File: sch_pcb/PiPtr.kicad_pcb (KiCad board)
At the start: 4 copper layers, 101.6 x 141.7 mm, 383 parts, among them J101 GLOBAL_LINK_LEFT, J102 GLOBAL_LINK_RIGHT, J107 RASPBERRY_PI, J111 FP_PIXEL, J112 AM2302, J204 DE9F, J305 AUX_IO_1, J307 SPARE, J308 AUX_IO_2, J311 I2C1_5V, J312 RTC, J315 OLED_SSD1306, J404 DE9F, J501 MicroUSB, P301 Chassis, Q101 BSS138, Q102 BSS138, Q103 BSS138, Q104 BSS138, Q105 BSS138, Q201 BSS138, Q202 BSS138, Q203 BSS138, Q401 BSS138, Q402 BSS138, Q403 BSS138, Q501 BSR315PH6327XTSA1, U101 MCP23008, U102 IP4234CZ6, U103 MCP4351, U104 74HCT138, U105 74LV1T125, U106 MCP6004T, U107 MCP4351, U108 74LVC4066, U109 74LVC1G3157, U110 74LV1T125, U111 74LV1T125, U112 74LV1T125, U113 74LV1T125, U201 MCP6004T, U202 74LVC1G3157, U203 74LVC1G3157, U204 74LVC4066, U205 MCP6004T, U206 74LVC1G3157, U207 MCP6S26, U208 MCP23008, U301 MCP23017, U304 MCP3008, U305 MCP1703A-2502/MB, U306 TPS54302, U307 IP4234CZ6, U308 IP4234CZ6, U401 MCP6004T, U402 74LVC1G3157, U403 74LVC1G3157, U404 74LVC4066, U405 MCP6004T, U406 74LVC1G3157, U407 MCP6S26, U408 MCP23008, U501 CM108B, U502 CM108B, U503 TUSB2036, U504 MCP1703A-3302/MB, U505 CM108B, Y501 6MHz

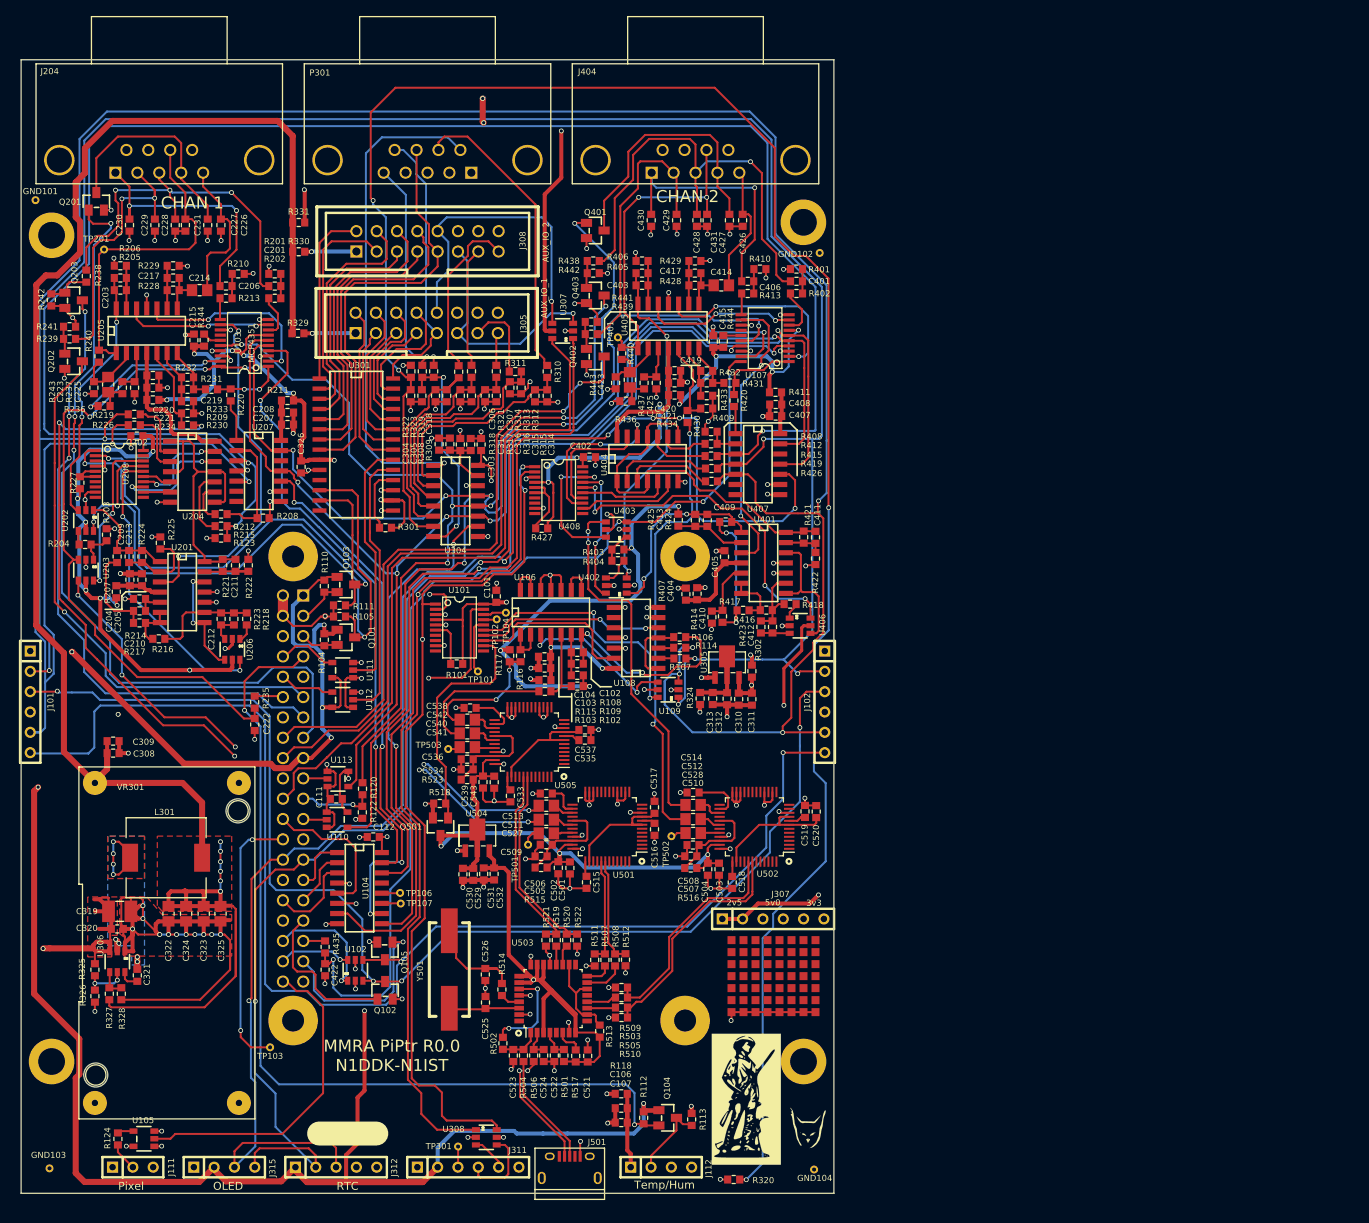
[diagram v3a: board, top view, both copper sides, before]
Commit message: Add files via upload
Fix i2c addressing
Change footprint for LDR
Move connectors for temp/hum sensor and rtc so they won't hit the Pi
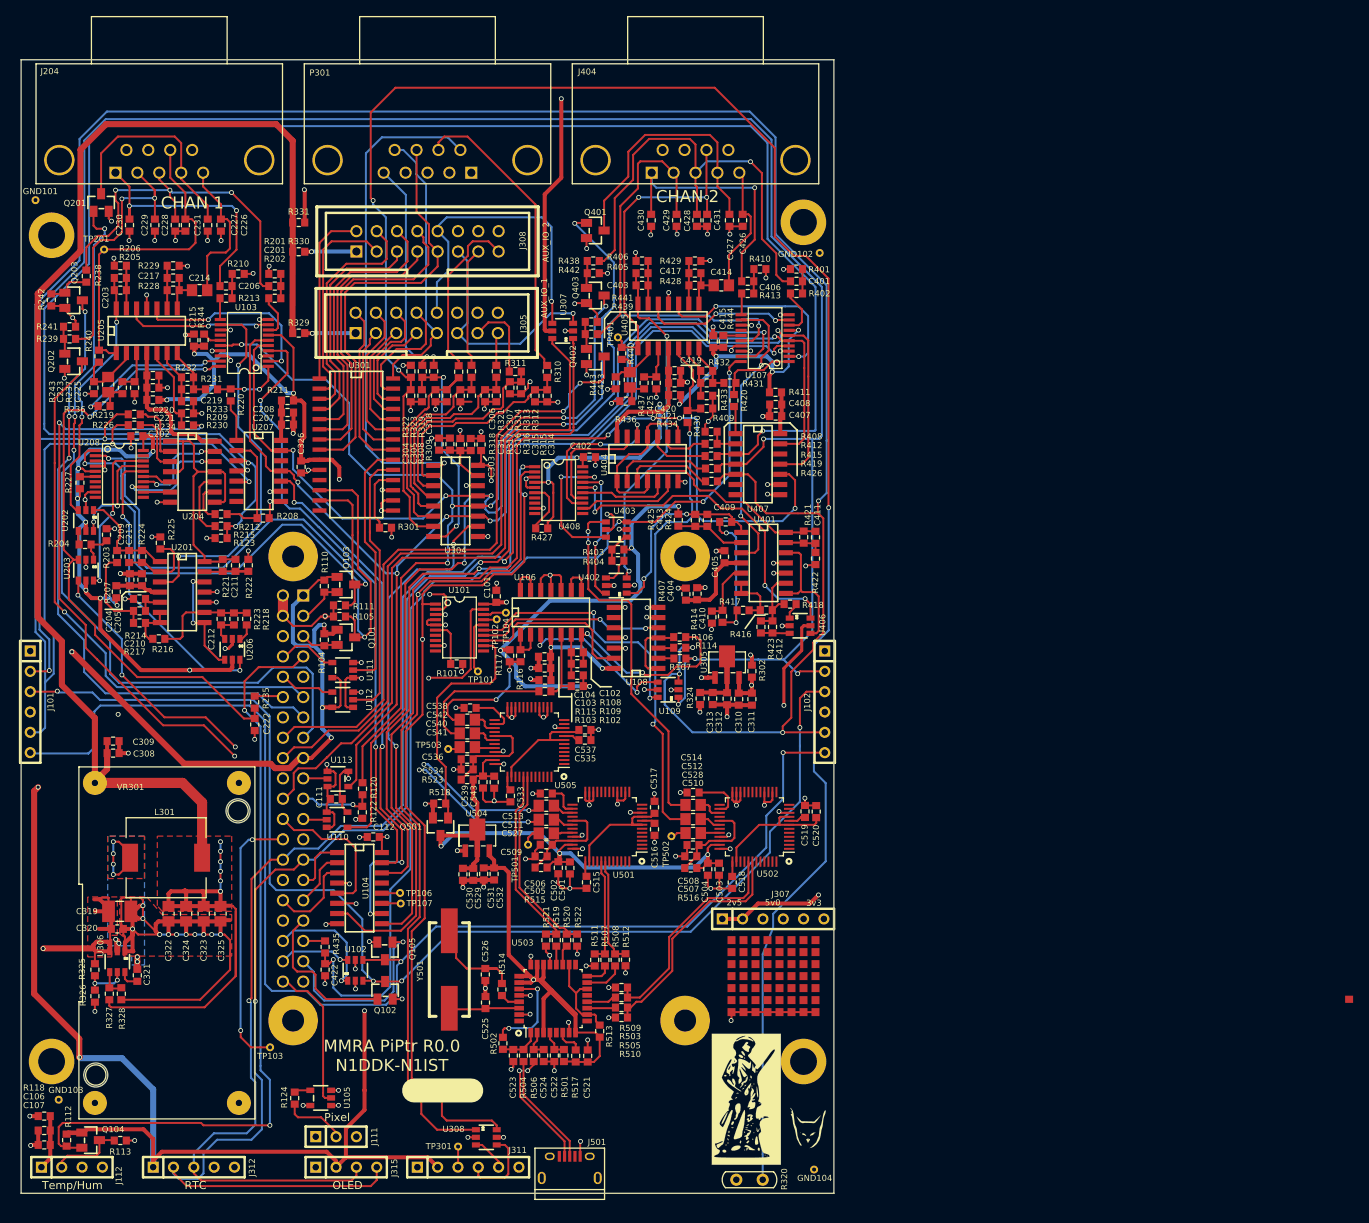
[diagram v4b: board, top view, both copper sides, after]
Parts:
- R216, R218, R416, R418: value 50k -> 51k
- R310, R311, R312, R313, R314, R321: value 90k -> 88k7
- R320: footprint lib:smd0603 -> lib:LDR
- moved J112 73.7 mm to (63.5, 166.4)
- moved C106 72.2 mm to (60.0, 161.8)
- moved C107 72.2 mm to (60.0, 163.6)
- moved Q104 72.2 mm to (65.8, 163.0)
- moved R112 72.2 mm to (62.8, 163.0)
- moved R118 72.2 mm to (60.0, 160.0)
- moved R113 71.5 mm to (69.5, 163.0), turned to 0 degrees
- moved J111 25.7 mm to (96.5, 162.6)
- moved R124 22.7 mm to (91.3, 157.7)
- moved U105 22.7 mm to (94.6, 157.7)
- moved J312 17.8 mm to (80.0, 166.4)
- moved J315 15.2 mm to (97.8, 166.4)
- moved GND103 8.65 mm to (61.9, 157.9)
- moved R320 1.98 mm to (148.2, 167.9), turned to 0 degrees
- moved Q201 0.62 mm to (67.2, 45.8)
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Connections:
- U101 pad 5: GND -> +5V
- U208 pad 5: Net-(R227-Pad1) -> +5V
- U301 pad 16: +5V -> GND
- U301 pad 17: GND -> +5V
- U408 pad 5: Net-(R427-Pad1) -> GND
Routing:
- net /SDA0_33: track 148.0 -> 173.9 mm
- net +3V3: track 561.9 -> 537.2 mm, vias 11 -> 9
- net /PIXEL_33: track 40.9 -> 19.3 mm
- net /DHT_33: track 113.4 -> 97.9 mm
- net /SCL0_33: track 154.3 -> 163.8 mm
- net +5V: track 531.0 -> 523.6 mm, vias 46 -> 47
- net Net-(J111-Pad2): track 3.55 -> 7.91 mm
- net /CH1/TONE_FROM_PI: track 83.4 -> 79.2 mm, vias 3 -> 2
- net GND: track 367.9 -> 370.4 mm, vias 155 -> 153
- net Net-(C106-Pad1): track 11.1 -> 8.64 mm
- net Net-(R227-Pad1): track 4.14 -> 1.93 mm
- net /Spares, GPIO, and ADC/ADC_LIGHT: track 251.8 -> 249.7 mm, vias 4 -> 3
- net Net-(R427-Pad1): track 8.46 -> 6.62 mm
- net /PTT1D: track 101.2 -> 99.3 mm
- net Net-(R208-Pad2): track 16.2 -> 14.5 mm
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
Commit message: Add Digikey part # to all parts.  Fix unconnected nets
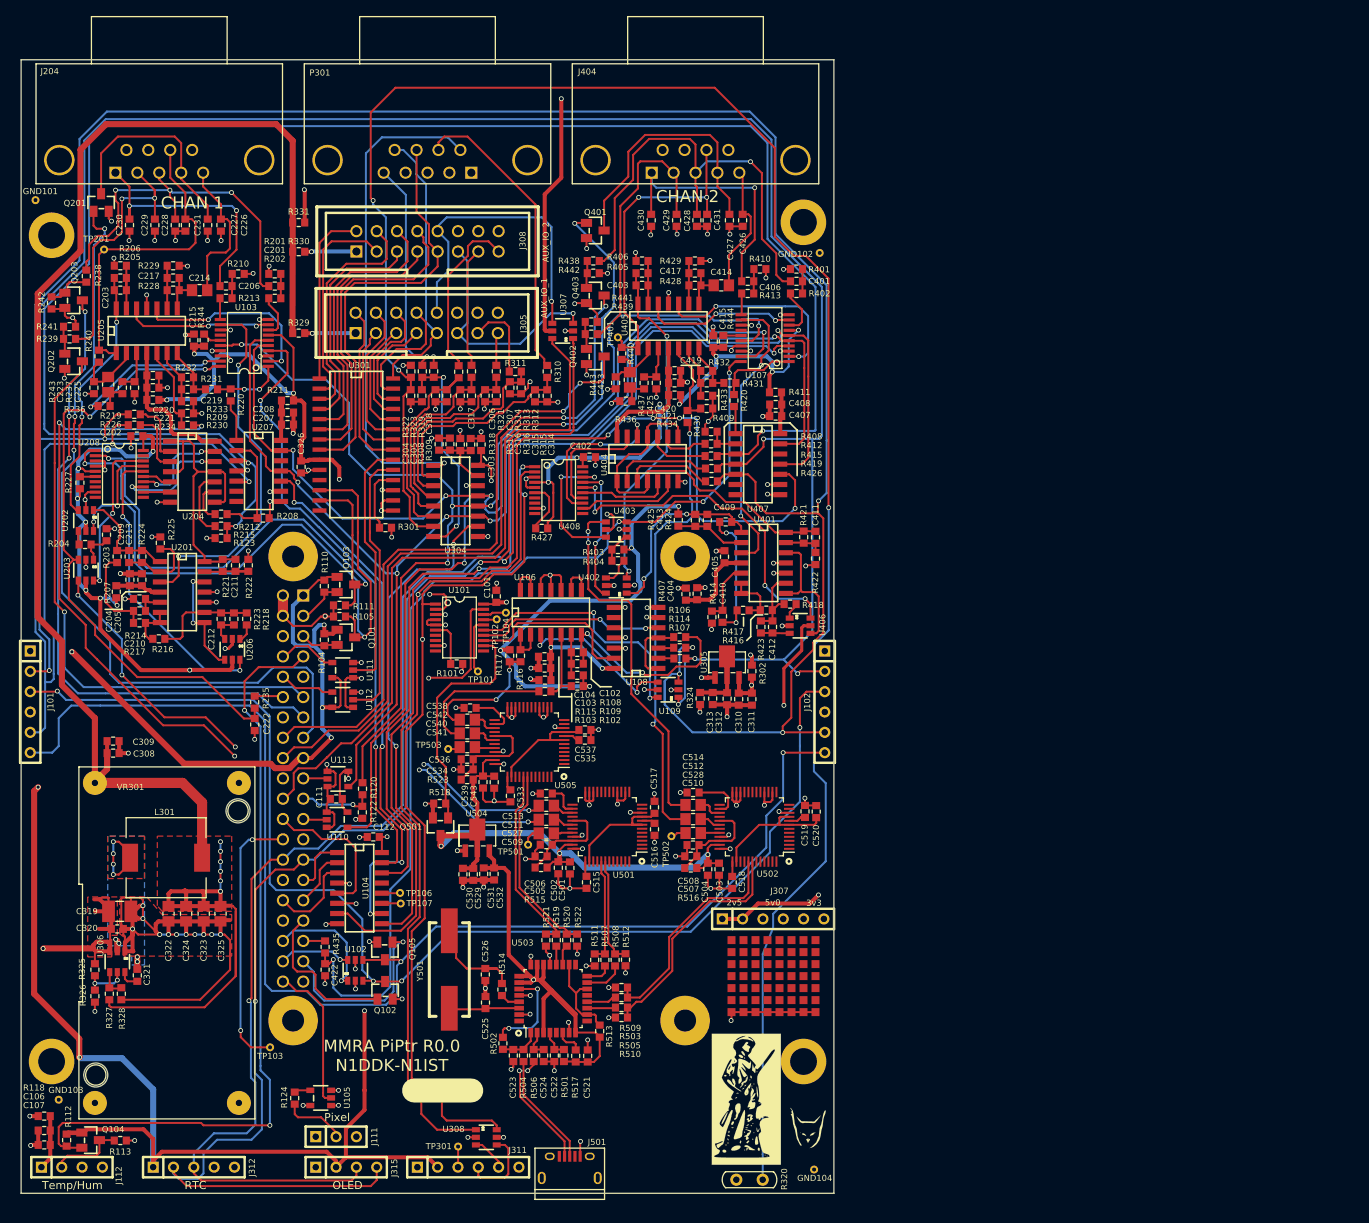
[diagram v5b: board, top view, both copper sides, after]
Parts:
- Q501: value BSR315PH6327XTSA1 -> NX2301P,215
- moved R242 0.38 mm to (61.0, 58.3)
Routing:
- net +2V5: track 152.7 -> 147.0 mm, vias 39 -> 38
- net +5V: track 523.6 -> 526.2 mm
- net /COR1: track 69.2 -> 71.6 mm
- net /~CTCSS1: track 79.1 -> 81.1 mm
- net GND: track 370.4 -> 371.4 mm

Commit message: Switch to 0402 parts and SeeedStudio footprints
Silk screen is still being updated.  BOM needs to be updated as well
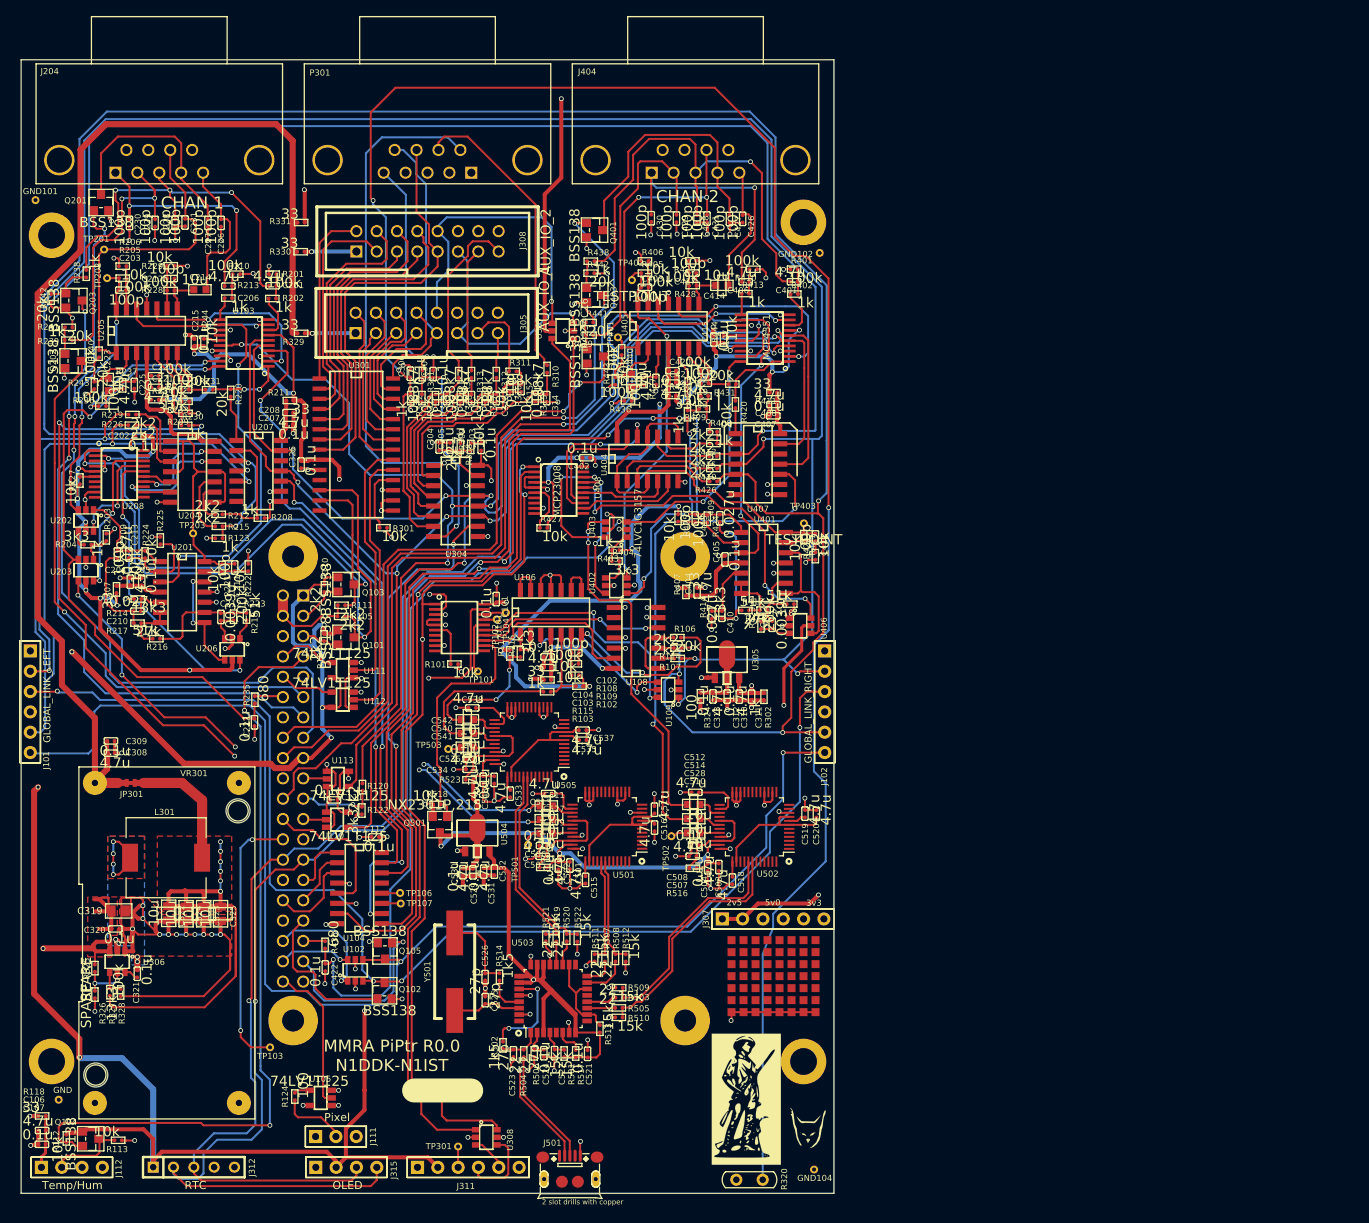
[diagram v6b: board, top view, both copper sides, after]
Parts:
- added JP301: 5V_switcher_connect, lib:JUMPER_2PIN_CUTTABLE, F.Cu at (70.8, 118.3)
- added TP202: TESTPOINT, lib:Wire_28AWG, F.Cu at (67.9, 55.2)
- added TP203: TESTPOINT, lib:Wire_28AWG, F.Cu at (78.7, 87.1)
- added TP402: TESTPOINT, lib:Wire_28AWG, F.Cu at (133.5, 55.5)
- added TP403: TESTPOINT, lib:Wire_28AWG, F.Cu at (155.0, 85.9)
- C101, C102, C103, C104, C106, C107, C111, C112, C201, C202, C203, C204, C205, C206, C207, C208, C209, C210, C211, C212, C213, C215, C217, C219, C220, C221, C222, C225, C226, C227, C228, C229, C230, C231, C303, C304, C305, C306, C307, C308, C309, C310, C311, C312, C313, C314, C315, C316, C317, C318, C320, C321, C326, C401, C402, C403, C404, C405, C406, C407, C408, C409, C410, C411, C412, C413, C415, C417, C419, C420, C421, C422, C425, C426, C427, C428, C429, C430, C431, C501, C502, C503, C504, C505, C506, C507, C508, C513, C514, C515, C516, C517, C518, C519, C520, C521, C522, C523, C524, C525, C526, C529, C530, C531, C532, C533, C534, C535, C536, C537, C538, C539, C543: footprint lib:smd0603 -> lib:OPL_C0402
- C214, C223, C414, C423, C509, C510, C511, C512, C527, C528, C540, C541, C542: footprint lib:smd0805 -> lib:OPL_C0603
- C319: footprint lib:smd1210 -> lib:OPL_C0805
- C322, C323, C324, C325: footprint lib:smd0805 -> lib:OPL_C0805
- J101, J102, J307, J311: footprint lib:SIL-6 -> lib:OPL_H6-2.54
- J111: footprint lib:SIL-3 -> lib:OPL_H3-2.54
- J112, J315: footprint lib:SIL-4 -> lib:OPL_H4-2.54
- J501: footprint lib:USB_Micro-B -> lib:OPL_MICRO-USB5+4P-SMD-0.65-B
- Q101, Q102, Q103, Q104, Q105, Q201, Q202, Q203, Q401, Q402, Q403, Q501: footprint lib:SOT23 -> lib:OPL_SOT-23
- R101, R102, R103, R104, R105, R106, R107, R108, R109, R110, R111, R112, R113, R114, R115, R116, R117, R118, R120, R122, R123, R124, R201, R202, R203, R204, R205, R206, R207, R208, R209, R210, R211, R212, R213, R214, R215, R216, R217, R218, R219, R220, R221, R222, R223, R224, R225, R226, R227, R228, R229, R230, R231, R232, R233, R234, R235, R236, R237, R238, R239, R240, R241, R242, R243, R244, R301, R302, R308, R309, R310, R311, R312, R313, R314, R315, R316, R317, R318, R319, R321, R322, R323, R324, R325, R326, R327, R328, R329, R330, R331, R401, R402, R403, R404, R405, R406, R407, R408, R409, R410, R411, R412, R413, R414, R415, R416, R417, R418, R419, R420, R421, R422, R423, R424, R425, R426, R427, R428, R429, R430, R431, R432, R433, R434, R435, R436, R437, R438, R439, R440, R441, R442, R443, R444, R501, R502, R503, R504, R505, R506, R507, R508, R509, R510, R511, R512, R513, R514, R515, R516, R517, R518, R519, R520, R521, R522, R523: footprint lib:smd0603 -> lib:OPL_R0402
- U101, U103, U107, U208, U408: footprint lib:SSOP-20 -> lib:OPL_TSSOP20-0.65-6.5X4.4MM
- U102, U109, U202, U203, U206, U306, U307, U308, U402, U403, U406: footprint lib:SOT23-6 -> lib:OPL_SOT-23-6
- U105, U110, U111, U112, U113: footprint lib:SOT23-5 -> lib:OPL_SOT-23-5
- U305, U504: footprint lib:sot89 -> lib:OPL_SOT-89
- moved R302 3.54 mm to (150.0, 107.6), turned to 0 degrees
- moved J501 1.68 mm to (125.8, 164.7)
- moved R514 1.61 mm to (117.0, 142.6), turned to 180 degrees
- moved C409 0.87 mm to (144.5, 85.3)
- moved R410 0.83 mm to (148.7, 54.1), turned to 270 degrees
- moved Y501 0.73 mm to (111.3, 141.9)
- moved R242 0.65 mm to (60.9, 57.7), turned to 0 degrees
- moved R420 0.53 mm to (146.4, 71.0), turned to 0 degrees
- moved R224 0.47 mm to (72.7, 89.8), turned to 0 degrees
- moved R409 0.47 mm to (142.4, 71.6), turned to 270 degrees
- moved C403 0.44 mm to (135.1, 56.4), turned to 90 degrees
- moved C506 0.42 mm to (122.4, 126.2), turned to 270 degrees
- moved C402 0.41 mm to (127.8, 77.7), turned to 270 degrees
- moved R518 0.39 mm to (109.1, 121.0), turned to 270 degrees
- moved C104 0.39 mm to (123.0, 102.6), turned to 270 degrees
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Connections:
- C322 pad 1: +5V -> Net-(C322-Pad1)
- C323 pad 1: +5V -> Net-(C322-Pad1)
- C324 pad 1: +5V -> Net-(C322-Pad1)
- C325 pad 1: +5V -> Net-(C322-Pad1)
- J305 pad 16: Net-(J305-Pad16) -> (no net)
- J308 pad 16: Net-(J308-Pad16) -> (no net)
- J312 pad 4: (no net) -> Net-(J312-Pad4)
- L301 pad 1: +5V -> Net-(C322-Pad1)
- MTG301 pad 1: Net-(MTG301-Pad1) -> (no net)
- MTG302 pad 1: Net-(MTG302-Pad1) -> (no net)
- MTG303 pad 1: Net-(MTG303-Pad1) -> (no net)
- MTG304 pad 1: Net-(MTG304-Pad1) -> (no net)
- R327 pad 1: +5V -> Net-(C322-Pad1)
- U101 pad 10: (no net) -> Net-(U101-Pad10)
- U101 pad 11: (no net) -> Net-(U101-Pad11)
- U101 pad 7: (no net) -> Net-(U101-Pad7)
- U101 pad 8: (no net) -> Net-(U101-Pad8)
- U104 pad 13: Net-(U104-Pad13) -> (no net)
- U108 pad 10: (no net) -> Net-(U108-Pad10)
- U108 pad 9: (no net) -> Net-(U108-Pad9)
- U207 pad 12: Net-(U207-Pad12) -> (no net)
- U207 pad 6: Net-(U207-Pad6) -> (no net)
- U207 pad 7: Net-(U207-Pad7) -> (no net)
- U208 pad 10: (no net) -> Net-(U208-Pad10)
- U208 pad 11: (no net) -> Net-(U208-Pad11)
- U208 pad 19: (no net) -> Net-(U208-Pad19)
- U208 pad 7: (no net) -> Net-(U208-Pad7)
- U208 pad 8: (no net) -> Net-(U208-Pad8)
- U407 pad 12: Net-(U407-Pad12) -> (no net)
- U407 pad 6: Net-(U407-Pad6) -> (no net)
- U407 pad 7: Net-(U407-Pad7) -> (no net)
- U501 pad 1: Net-(U501-Pad1) -> (no net)
- U501 pad 11: Net-(U501-Pad11) -> (no net)
- U501 pad 12: Net-(U501-Pad12) -> (no net)
- U501 pad 13: Net-(U501-Pad13) -> (no net)
- U501 pad 15: Net-(U501-Pad15) -> (no net)
- U501 pad 17: Net-(U501-Pad17) -> (no net)
- U501 pad 18: Net-(U501-Pad18) -> (no net)
- U501 pad 19: Net-(U501-Pad19) -> (no net)
- U501 pad 2: Net-(U501-Pad2) -> (no net)
- U501 pad 20: Net-(U501-Pad20) -> (no net)
- U501 pad 21: Net-(U501-Pad21) -> (no net)
- U501 pad 25: Net-(U501-Pad25) -> (no net)
- U501 pad 28: Net-(U501-Pad28) -> (no net)
- U501 pad 3: Net-(U501-Pad3) -> (no net)
- U501 pad 31: Net-(U501-Pad31) -> (no net)
- U501 pad 39: Net-(U501-Pad39) -> (no net)
- U501 pad 4: Net-(U501-Pad4) -> (no net)
- U501 pad 40: Net-(U501-Pad40) -> (no net)
- U501 pad 43: Net-(U501-Pad43) -> (no net)
- U501 pad 44: Net-(U501-Pad44) -> (no net)
- U501 pad 45: Net-(U501-Pad45) -> (no net)
- U501 pad 46: Net-(U501-Pad46) -> (no net)
- U501 pad 47: Net-(U501-Pad47) -> (no net)
- U501 pad 48: Net-(U501-Pad48) -> (no net)
- U501 pad 5: Net-(U501-Pad5) -> (no net)
- U501 pad 6: Net-(U501-Pad6) -> (no net)
- U502 pad 1: Net-(U502-Pad1) -> (no net)
- U502 pad 11: Net-(U502-Pad11) -> (no net)
- U502 pad 12: Net-(U502-Pad12) -> (no net)
- U502 pad 13: Net-(U502-Pad13) -> (no net)
- U502 pad 15: Net-(U502-Pad15) -> (no net)
- U502 pad 17: Net-(U502-Pad17) -> (no net)
- U502 pad 18: Net-(U502-Pad18) -> (no net)
- U502 pad 19: Net-(U502-Pad19) -> (no net)
- U502 pad 2: Net-(U502-Pad2) -> (no net)
- U502 pad 20: Net-(U502-Pad20) -> (no net)
- U502 pad 21: Net-(U502-Pad21) -> (no net)
- U502 pad 25: Net-(U502-Pad25) -> (no net)
- U502 pad 28: Net-(U502-Pad28) -> (no net)
- U502 pad 3: Net-(U502-Pad3) -> (no net)
- U502 pad 31: Net-(U502-Pad31) -> (no net)
- U502 pad 39: Net-(U502-Pad39) -> (no net)
- U502 pad 4: Net-(U502-Pad4) -> (no net)
- U502 pad 40: Net-(U502-Pad40) -> (no net)
- U502 pad 43: Net-(U502-Pad43) -> (no net)
- U502 pad 44: Net-(U502-Pad44) -> (no net)
- U502 pad 45: Net-(U502-Pad45) -> (no net)
- U502 pad 46: Net-(U502-Pad46) -> (no net)
- U502 pad 47: Net-(U502-Pad47) -> (no net)
- U502 pad 48: Net-(U502-Pad48) -> (no net)
- U502 pad 5: Net-(U502-Pad5) -> (no net)
- U502 pad 6: Net-(U502-Pad6) -> (no net)
- U503 pad 13: Net-(U503-Pad13) -> (no net)
- U503 pad 17: Net-(U503-Pad17) -> (no net)
- U503 pad 32: Net-(U503-Pad32) -> (no net)
- U503 pad 5: Net-(U503-Pad5) -> (no net)
- U503 pad 9: Net-(U503-Pad9) -> (no net)
- U505 pad 1: (no net) -> Net-(U505-Pad1)
- U505 pad 11: (no net) -> Net-(U505-Pad11)
- U505 pad 12: (no net) -> Net-(U505-Pad12)
- U505 pad 13: (no net) -> Net-(U505-Pad13)
- U505 pad 15: (no net) -> Net-(U505-Pad15)
- U505 pad 17: (no net) -> Net-(U505-Pad17)
- U505 pad 18: (no net) -> Net-(U505-Pad18)
- U505 pad 19: (no net) -> Net-(U505-Pad19)
- U505 pad 2: (no net) -> Net-(U505-Pad2)
- U505 pad 20: (no net) -> Net-(U505-Pad20)
- U505 pad 21: (no net) -> Net-(U505-Pad21)
- U505 pad 25: (no net) -> Net-(U505-Pad25)
- U505 pad 28: (no net) -> Net-(U505-Pad28)
- U505 pad 3: (no net) -> Net-(U505-Pad3)
- U505 pad 31: (no net) -> Net-(U505-Pad31)
- U505 pad 39: (no net) -> Net-(U505-Pad39)
- U505 pad 4: (no net) -> Net-(U505-Pad4)
- U505 pad 40: (no net) -> Net-(U505-Pad40)
- U505 pad 43: (no net) -> Net-(U505-Pad43)
- U505 pad 44: (no net) -> Net-(U505-Pad44)
- U505 pad 45: (no net) -> Net-(U505-Pad45)
- U505 pad 46: (no net) -> Net-(U505-Pad46)
- U505 pad 47: (no net) -> Net-(U505-Pad47)
- U505 pad 48: (no net) -> Net-(U505-Pad48)
- U505 pad 5: (no net) -> Net-(U505-Pad5)
- U505 pad 6: (no net) -> Net-(U505-Pad6)
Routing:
- net Net-(C322-Pad1): track 0.00 -> 80.4 mm, vias 0 -> 6
- net +5V: track 526.2 -> 453.5 mm, vias 47 -> 41
- net GND: track 371.4 -> 398.8 mm
- net +2V5: track 147.0 -> 153.0 mm
- net /COR1: track 71.6 -> 69.2 mm
- net Net-(C223-Pad2): track 8.68 -> 11.0 mm
- net Net-(C423-Pad2): track 8.46 -> 10.7 mm
- net Net-(C318-Pad1): track 25.8 -> 23.6 mm
- net Net-(R514-Pad1): track 2.48 -> 4.68 mm
- net Net-(C213-Pad2): track 10.2 -> 12.4 mm
- net /~CTCSS1: track 81.1 -> 79.1 mm
- net Net-(C106-Pad1): track 8.64 -> 6.69 mm
- net Net-(C403-Pad1): track 42.9 -> 44.7 mm
- net /CH1/VDDA_2: track 18.1 -> 19.9 mm
- net Net-(C511-Pad2): track 2.68 -> 4.33 mm
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- added copper zone on F.Cu, net Net-(C322-Pad1)
- removed copper zone on F.Cu, net +5V
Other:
- board text added: "GND"
